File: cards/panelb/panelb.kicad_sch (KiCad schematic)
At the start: 111 parts, among them J1 BUS, Q1 2N7000, Q10 2N7000, Q11 2N7000, Q12 2N7000, Q13 2N7000, Q14 2N7000, Q15 2N7000, Q16 2N7000, Q17 2N7000, Q18 2N7000, Q19 2N7000, Q2 2N7000, Q20 2N7000, Q3 2N7000, Q4 2N7000, Q5 2N7000, Q6 2N7000, Q7 2N7000, Q8 2N7000, Q9 2N7000, SW1 OI IO II PCE PCL FI HLT MAI (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, SW2 MI MO WRL WRH ONE F0 F1 INP, SW3 CLK, SW4 RST

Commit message: Clock and panel: CLK and RST driven hard, the cards see one clock edge (D053)
The memory address latch race (D054, next commit) had a root under it:
the clock card's CLK pull-up was 10k into about 3 nF of card inputs and
ribbon, so the rising edge took 35 to 43 us from 0.5 to 3.5 V, and every
card reads that edge with its own transistors (Vto 0.8 to 3.0 V), so the
cards saw one edge up to 25 us apart. At mixed seed 2 the sequencer stepped
at 2 V and a register put the next tick's data on the bus 10 us later,
while the memory control card saw the edge at 3 V, 12 us after the bus had
changed. RST had the same trouble the other way: driven through 10k
against the panel's 1 Meg, it drifted for 8 ms after the reset Schmitt
let go (the machine once started a tick late, memory nibble-v2-plan
2026-09-14), so cards with different thresholds left reset on different
edges.

cards/clock (re-routed, DRC 0, 0 unconnected): the CLK pull-up is 1k, and
RST comes from a new inverter RD = NOT PB with a 1k pull-up through 100 ohm
and a diode. Lowering PA's own 47k instead took the gain out of the reset
Schmitt and RST followed the 220 ms capacitor ramp for milliseconds; the
buffer keeps the snap. cards/panela, panelb (values only, no layout
change): the CLK and RST pull-downs are 10k, the buttons' Schmitt output
inverters have 1k pull-ups and drive the lines through 100 ohm. About
20 mA more from the supply.

tb_clock now loads both lines with 3 nF and the panel's 10k, drives the
STEP button as the panel does, and measures CLK's rise (0.5 to 3.5 V,
must be under 10 us) and RST's release (3.5 to 0.8 V, under 100 us). On
the routed card's export: CLK rise 5.3 to 6.7 us, RST release 44 to 46 us,
period and duty unchanged (610 Hz TYP, 404 LO, 582 HI), one edge per STEP
press, at TYP, LO, HI, MIX 1 and 2, all PASS (sim/out/tb_clock_cards54_*.log).
The previous card on the same bench: CLK rise 43 us, RST never reached
0.8 V cleanly (sim/out/tb_clock_cards_oldD053_TYP.log).

machine.py: a dec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
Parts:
- R18, R20: value 47k -> 1k
- R57, R62: value 10k -> 100
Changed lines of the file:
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@@
 			)
 		)
-		(property "Value" "47k"
+		(property "Value" "1k"
 			(at 88.9 237.49 0)
 			(show_name no)
@@
 			)
 		)
-		(property "Value" "47k"
+		(property "Value" "1k"
 			(at 165.1 237.49 0)
 			(show_name no)
@@
 			)
 		)
-		(property "Value" "10k"
+		(property "Value" "100"
 			(at 245.11 361.95 0)
 			(show_name no)
@@
 			)
 		)
-		(property "Value" "10k"
+		(property "Value" "100"
 			(at 245.11 392.43 0)
 			(show_name no)

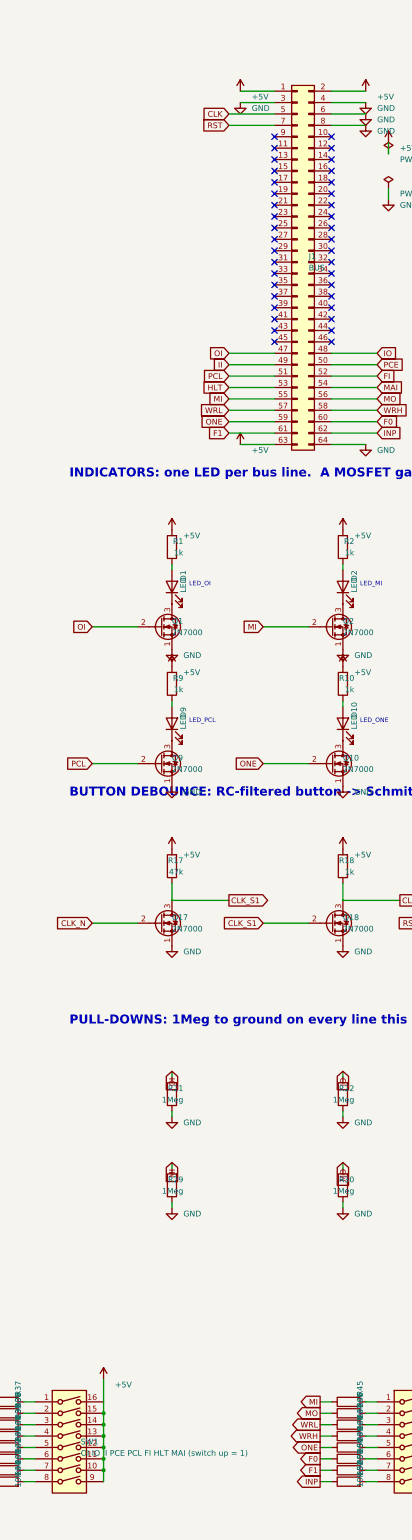
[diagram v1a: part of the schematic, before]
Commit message: The bus headers go on the back of all 26 boards, no track moved; the silkscreen refitted (D059, D062)
An IDC socket lies across its ribbon, so the ribbon could never run along a
row of cards as drawn. It runs behind them, and the 64-pin headers are
soldered on the back. This commit is that move, made in place on the routed
boards: no board was routed again.

How the header sits (D062): in the holes it had, turned over top to bottom,
notch toward the top edge. A pin of the odd row is then in the hole its even
neighbour had, so the two signals of every pair of pins change places: CLK
is pin 6, RST pin 8, +5V pins 1, 2 and 64. bus.py keeps both tables: PINS,
what the header's pins carry, and HOLES, what the copper was routed to.

The proof, on all 26 boards against 992a90f (sim/board_diff.py):
  netlist the same, element for element; every track, every via and every
  hole the same; each copper and mask layer differs by two pad shapes per
  header (pin 1's square went to the hole beside it, both on +5V) and the
  ground pour's outline round those two pads, nowhere else by more than a
  tenth of a micrometre.
sim/rebuild_check.py runs every builder into a scratch directory: each
writes the plan and the netlist that are committed, so a rebuild gives
this board. order_check.py --machine holds every pad of the 27 headers to
bus.py and requires them on the back.

What the move costs: on the ribbon RST had a ground conductor on both
sides; now one neighbour is BUS1#. tb_rst_neighbour.py puts the two lines
on the bench with every gate the routed boards hang on them: RST rises
0.28 to 0.43 V when BUS1# is released, against a lowest threshold of 0.8 V
(sim/results/rst_neighbour.md). The machine deck's crosstalk option now
couples the pins that are neighbours on the ribbon; the crosstalk stage of
the machine gate has to be run again on that order.

Silkscreen (pcb.fit_silk): every label to 1.0 mm where it has room, off
pads, vias, outlines and other labels, out from under the pa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
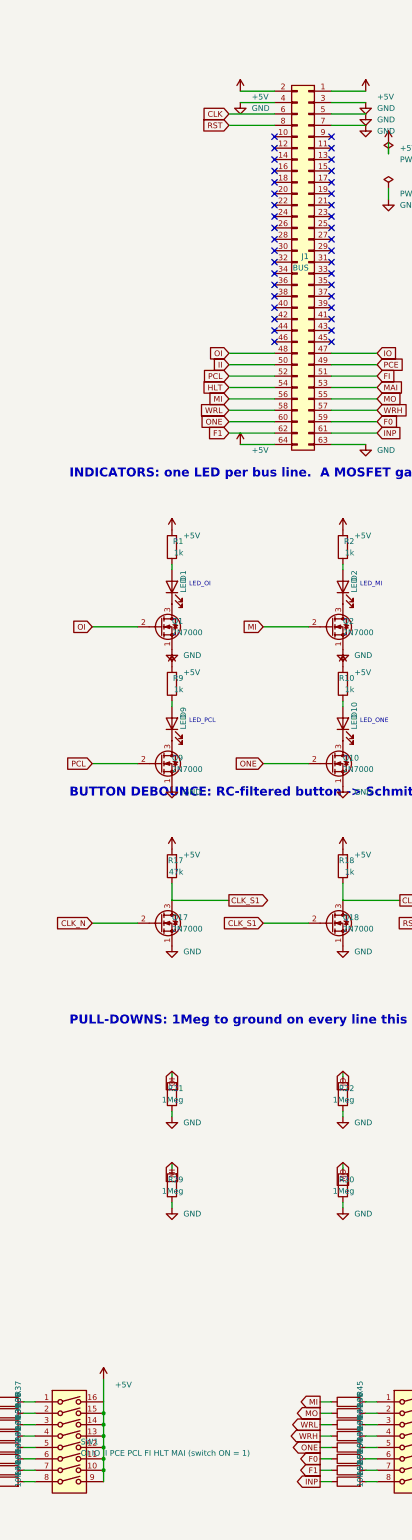
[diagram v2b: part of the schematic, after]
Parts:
- SW1: value OI IO II PCE PCL FI HLT MAI (switch up = 1) -> OI IO II PCE PCL FI HLT MAI (switch ON = 1)
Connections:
- net +5V: now also J1.64 (Pin_64); no longer J1.63 (Pin_63)
- net CLK: now also J1.6 (Pin_6); no longer J1.5 (Pin_5)
- net F0: now also J1.59 (Pin_59); no longer J1.60 (Pin_60)
- net F1: now also J1.62 (Pin_62); no longer J1.61 (Pin_61)
- net FI: now also J1.51 (Pin_51); no longer J1.52 (Pin_52)
- net GND: now also J1.5 (Pin_5), J1.63 (Pin_63), J1.7 (Pin_7); no longer J1.6 (Pin_6), J1.64 (Pin_64), J1.8 (Pin_8)
- net HLT: now also J1.54 (Pin_54); no longer J1.53 (Pin_53)
- net II: now also J1.50 (Pin_50); no longer J1.49 (Pin_49)
- net INP: now also J1.61 (Pin_61); no longer J1.62 (Pin_62)
- net IO: now also J1.47 (Pin_47); no longer J1.48 (Pin_48)
- net MAI: now also J1.53 (Pin_53); no longer J1.54 (Pin_54)
- net MI: now also J1.56 (Pin_56); no longer J1.55 (Pin_55)
- net MO: now also J1.55 (Pin_55); no longer J1.56 (Pin_56)
- net OI: now also J1.48 (Pin_48); no longer J1.47 (Pin_47)
- net ONE: now also J1.60 (Pin_60); no longer J1.59 (Pin_59)
- net PCE: now also J1.49 (Pin_49); no longer J1.50 (Pin_50)
- net PCL: now also J1.52 (Pin_52); no longer J1.51 (Pin_51)
- net RST: now also J1.8 (Pin_8); no longer J1.7 (Pin_7)
- net WRH: now also J1.57 (Pin_57); no longer J1.58 (Pin_58)
- net WRL: now also J1.58 (Pin_58); no longer J1.57 (Pin_57)
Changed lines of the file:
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@@
 	(symbol
 		(lib_id "Connector_Generic:Conn_02x32_Odd_Even")
-		(at 76.2 101.6 0)
+		(at 78.74 101.6 0)
+		(mirror y)
 		(unit 1)
 		(body_style 1)
@@
 			)
 		)
-		(property "Value" "OI IO II PCE PCL FI HLT MAI (switch up = 1)"
+		(property "Value" "OI IO II PCE PCL FI HLT MAI (switch ON = 1)"
 			(at 27.94 367.03 0)
 			(show_name no)
